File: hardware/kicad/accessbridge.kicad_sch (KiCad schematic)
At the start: 64 parts, among them J1 PWR+RELAY, J2 BELL+DPS, J3 Qwiic, J4 OUT, J5 EXP, Q1 AO3400A, SW1 PAIR, U1 AP63205WU-7, U2 XIAO_ESP32C6, U3 EL357N(C)(TA)-G, U4 EL357N(C)(TA)-G, U5 EL357N(C)(TA)-G, U6 CPC1014NTR

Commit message: HW-1.1 Rev B: USB-C power input; 3D-printable enclosure (DIN + wall)
- J6 power-only USB-C (5.1k CC, 500 mA PTC, SMAJ5.0A), diode-OR into the
  XIAO 5V pin and a new V_LOOP rail for the contact loops
- Board widened to 96 x 56 mm; Rev A placement and routing kept,
  incremental update/lock workflow in gen_pcb.py
- Regenerated fabrication data (HW-1.1 Rev B ZIP, BOM, CPL, renders, STEP)
- Parametric CadQuery enclosure: DIN-rail base, wall-screw base, lid,
  PAIR plunger, cable clamp; fit check against the PCB STEP; CI job
- Docs, tests plan and changelog updated

Co-Authored-By: Claude Opus 5.5 <noreply@anthropic.com>
Claude-Session: https://claude.ai/code/session_017ugbcLJnibWHxuv1cA2VcH
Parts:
- added C11: 10u/25V, Capacitor_SMD:C_0805_2012Metric, symbol Device:C
- added D13, D15, D16: SS14, Diode_SMD:D_SMA, symbol Device:D_Schottky
- added D14: SMAJ5.0A, Diode_SMD:D_SMA, symbol Diode:SMAJ5.0A
- added F2: 500mA/30V, Fuse:Fuse_1206_3216Metric, symbol Device:Polyfuse
- added J6: USB-C 5V, Connector_USB:USB_C_Receptacle_GCT_USB4125-xx-x_6P_TopMnt_Horizontal, symbol Connector:USB_C_Receptacle_PowerOnly_6P
- added R22, R23: 5.1k, Resistor_SMD:R_0603_1608Metric, symbol Device:R
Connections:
- net +12V: now also D15.2 (A); no longer R10.1, R14.1, R18.1
- net +5V_XIAO: now also D13.1 (K)
- net GND: now also C11.2, D14.2 (A2), J6.A12 (GND), J6.B12 (GND), J6.S1 (SHIELD), R22.2, R23.2
- new net CC1: J6.A5 (CC1), R22.1
- new net CC2: J6.B5 (CC2), R23.1
- new net VBUS: F2.1, J6.A9 (VBUS), J6.B9 (VBUS)
- new net VBUS_F: C11.1, D13.2 (A), D14.1 (A1), D16.2 (A), F2.2
- new net V_LOOP: D15.1 (K), D16.1 (K), R10.1, R14.1, R18.1
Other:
- note added: "CONTACT INPUTS: opto loops powered from V_LOOP (+12 V or USB 5 V)"
- note added: "Field loops: V_LOOP -> 2.2k -> opto LED -> COM ... contact ... NO -> 1k -> GND (~3.3 mA at 12 V, ~1.1 mA on USB)."
- note added: "J6 USB-C (Rev B): 5 V power only, no data. Firmware upload uses the XIAO's own USB-C."
- note added: "USB-C POWER INPUT 5 V (power only, Rev B)"
- note added: "VBUS -> F2 -> D13 -> +5V_XIAO (OR with D3) and D16 -> V_LOOP (OR with D15 from +12V). J4 OUT+ is 12 V only."
- note removed: "CONTACT INPUTS: opto loops powered from board +12 V (no external voltage)"
- note removed: "Field loops: +12V -> 2.2k -> opto LED -> COM ... contact ... NO -> 1k -> GND (~3.3 mA)."

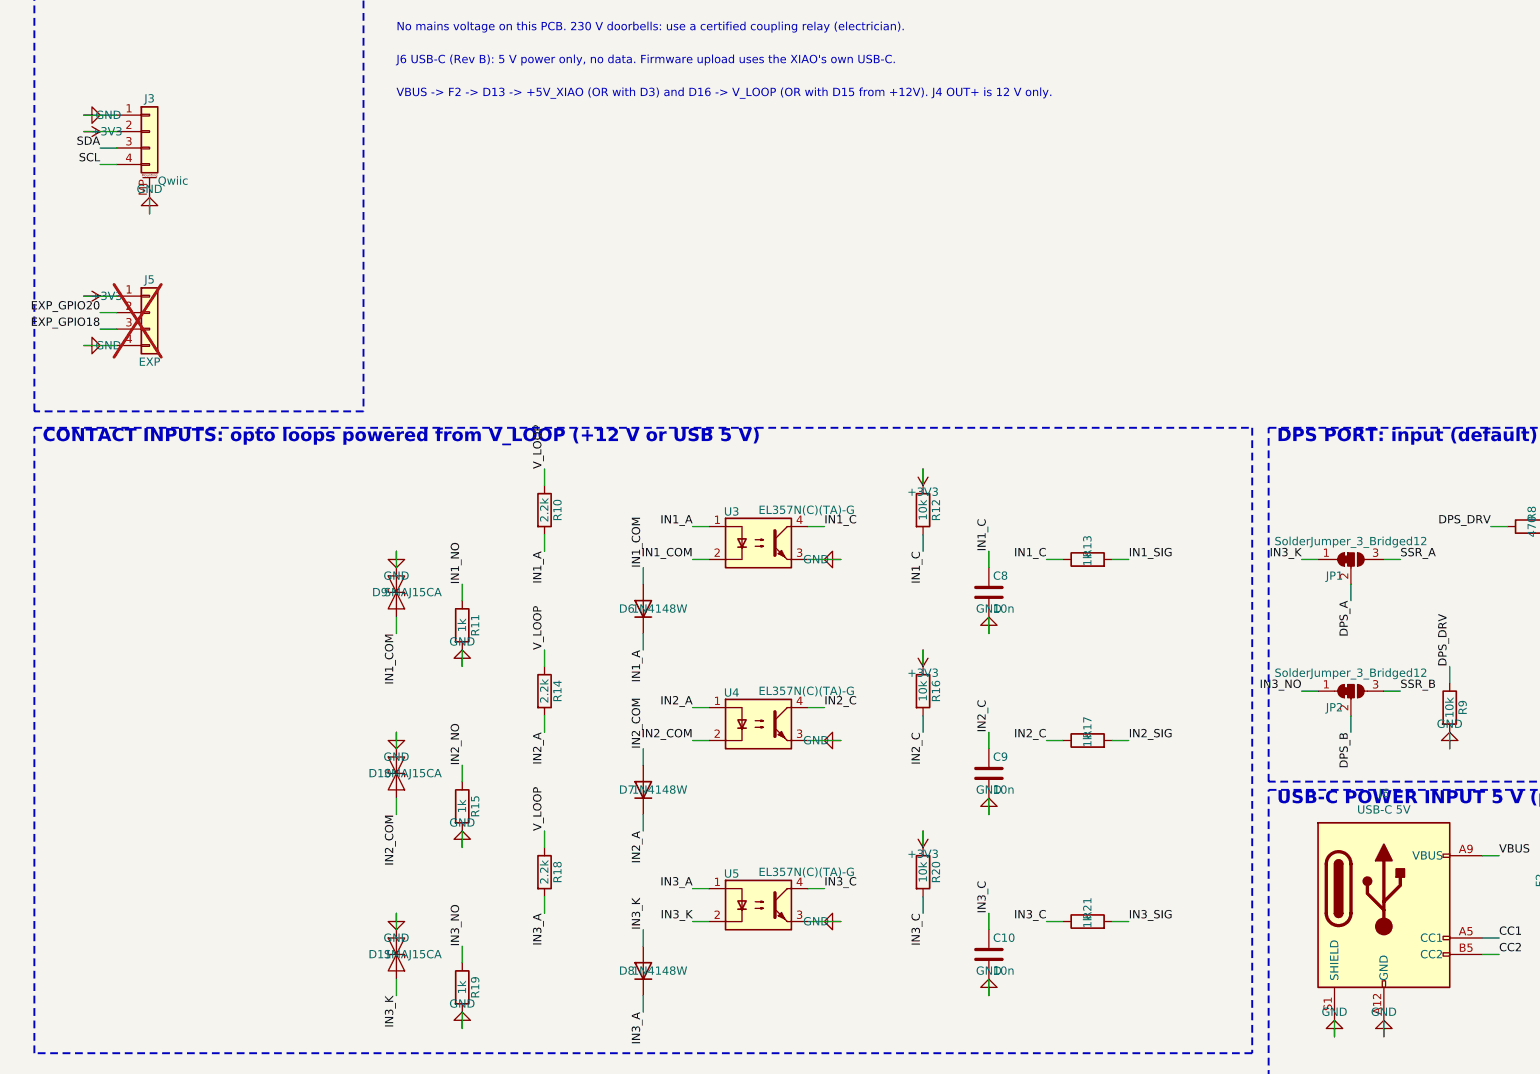
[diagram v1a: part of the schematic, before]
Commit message: Doorbell: any-source blueprint, no-neutral wiring options; wetting-current jumpers
- doorbell-notify blueprint accepts the AccessBridge counter, an event entity
  (e.g. Shelly input) or a binary sensor (e.g. battery Zigbee contact sensor);
  restore/reconnect ignored, optional event-type filter; 3 new tests (15/15)
- wiring.md: doorbell routes for 230 V bells without neutral at the push
  (coupling relay at the bell + battery Zigbee sensor, or cable to J2);
  Shelly 1L/2L and Eltako ER61-UC limitations documented
- Rev B (not manufactured): JP3-JP5 + R24-R26 (1k 1206, C4410) select ~3.3 or
  ~6 mA loop current per input; incremental routing, ERC/DRC clean incl. parity
- Regenerated fabrication data, renders, PCB STEP; enclosure fit check passes

Co-Authored-By: Claude Opus 5.5 <noreply@anthropic.com>
Claude-Session: https://claude.ai/code/session_017ugbcLJnibWHxuv1cA2VcH
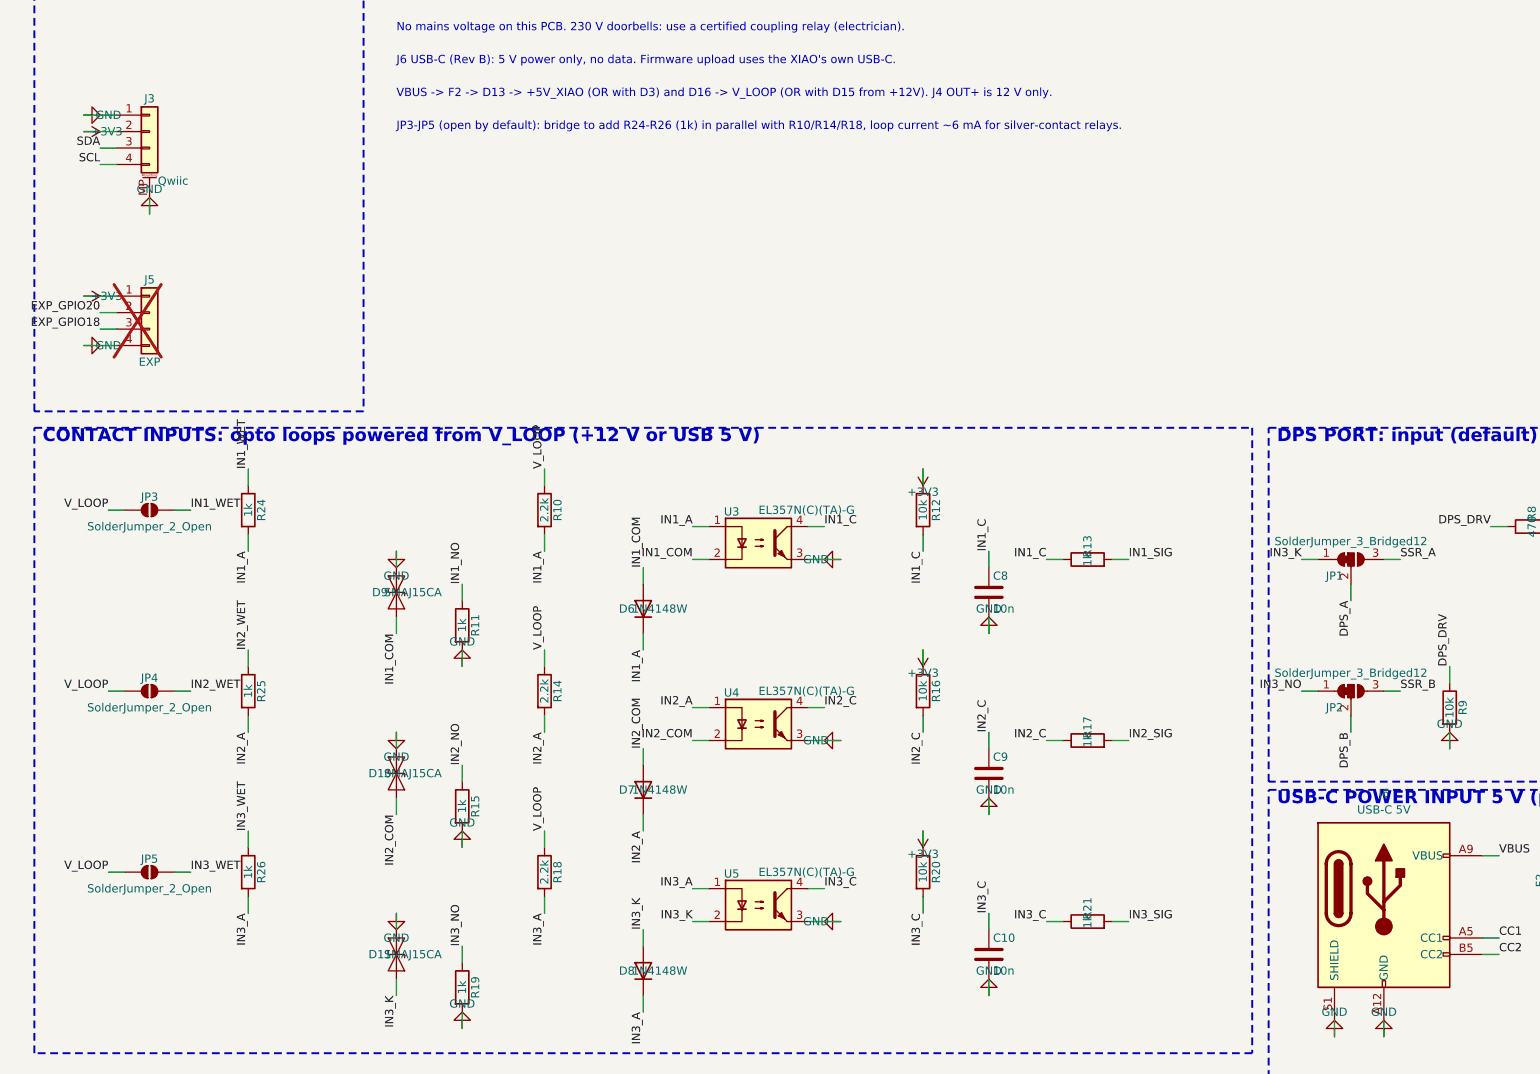
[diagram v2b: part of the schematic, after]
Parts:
- added JP3, JP4, JP5: SolderJumper_2_Open, Jumper:SolderJumper-2_P1.3mm_Open_RoundedPad1.0x1.5mm, symbol Jumper:SolderJumper_2_Open
- added R24, R25, R26: 1k, Resistor_SMD:R_1206_3216Metric, symbol Device:R
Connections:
- net IN1_A: now also R24.2
- net IN2_A: now also R25.2
- net IN3_A: now also R26.2
- net V_LOOP: now also JP3.1 (A), JP4.1 (A), JP5.1 (A)
- new net IN1_WET: JP3.2 (B), R24.1
- new net IN2_WET: JP4.2 (B), R25.1
- new net IN3_WET: JP5.2 (B), R26.1
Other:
- note added: "JP3-JP5 (open by default): bridge to add R24-R26 (1k) in parallel with R10/R14/R18, loop current ~6 mA for silver-contact relays."

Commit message: BOM: R8 470R = UNI-ROYAL 0603WAF4700T5E (C23179)
Co-Authored-By: Claude Opus 5.5 <noreply@anthropic.com>
Claude-Session: https://claude.ai/code/session_017ugbcLJnibWHxuv1cA2VcH
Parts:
- R8: LCSC (none) -> C23179; LCSC_Status unverified -> confirmed; MPN 0603 470R 1% thick film -> 0603WAF4700T5E; Manufacturer generic -> UNI-ROYAL
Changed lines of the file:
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@@
 			)
 		)
-		(property "MPN" "0603 470R 1% thick film"
+		(property "MPN" "0603WAF4700T5E"
 			(at 243.84 200.66 0)
 			(effects
@@
 			)
 		)
-		(property "Manufacturer" "generic"
+		(property "Manufacturer" "UNI-ROYAL"
 			(at 243.84 200.66 0)
 			(effects
@@
 			)
 		)
-		(property "LCSC" ""
+		(property "LCSC" "C23179"
 			(at 243.84 200.66 0)
 			(effects
@@
 			)
 		)
-		(property "LCSC_Status" "unverified"
+		(property "LCSC_Status" "confirmed"
 			(at 243.84 200.66 0)
 			(effects

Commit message: BOM: optocouplers U3-U5 = UMW EL357C (C725794); sync footprint values on update
Co-Authored-By: Claude Opus 5.5 <noreply@anthropic.com>
Claude-Session: https://claude.ai/code/session_017ugbcLJnibWHxuv1cA2VcH
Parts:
- U3, U4, U5: value EL357N(C)(TA)-G -> EL357C; LCSC C29981 -> C725794; MPN EL357N(C)(TA)-G -> EL357C; Manufacturer Everlight -> UMW
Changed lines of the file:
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@@
 			)
 		)
-		(property "Value" "EL357N(C)(TA)-G"
+		(property "Value" "EL357C"
 			(at 124.46 198.12 0)
 			(effects
@@
 			)
 		)
-		(property "MPN" "EL357N(C)(TA)-G"
+		(property "MPN" "EL357C"
 			(at 124.46 203.2 0)
 			(effects
@@
 			)
 		)
-		(property "Manufacturer" "Everlight"
+		(property "Manufacturer" "UMW"
 			(at 124.46 203.2 0)
 			(effects
@@
 			)
 		)
-		(property "LCSC" "C29981"
+		(property "LCSC" "C725794"
 			(at 124.46 203.2 0)
 			(effects
@@
 			)
 		)
-		(property "Value" "EL357N(C)(TA)-G"
+		(property "Value" "EL357C"
 			(at 124.46 226.06 0)
 			(effects
@@
 			)
 		)
-		(property "MPN" "EL357N(C)(TA)-G"
+		(property "MPN" "EL357C"
 			(at 124.46 231.14 0)
 			(effects
@@
 			)
 		)
-		(property "Manufacturer" "Everlight"
+		(property "Manufacturer" "UMW"
 			(at 124.46 231.14 0)
 			(effects
@@
 			)
 		)
-		(property "LCSC" "C29981"
+		(property "LCSC" "C725794"
 			(at 124.46 231.14 0)
 			(effects
@@
 			)
 		)
-		(property "Value" "EL357N(C)(TA)-G"
+		(property "Value" "EL357C"
 			(at 124.46 254 0)
 			(effects
@@
 			)
 		)
-		(property "MPN" "EL357N(C)(TA)-G"
+		(property "MPN" "EL357C"
 			(at 124.46 259.08 0)
 			(effects
@@
 			)
 		)
-		(property "Manufacturer" "Everlight"
+		(property "Manufacturer" "UMW"
 			(at 124.46 259.08 0)
 			(effects
@@
 			)
 		)
-		(property "LCSC" "C29981"
+		(property "LCSC" "C725794"
 			(at 124.46 259.08 0)
 			(effects

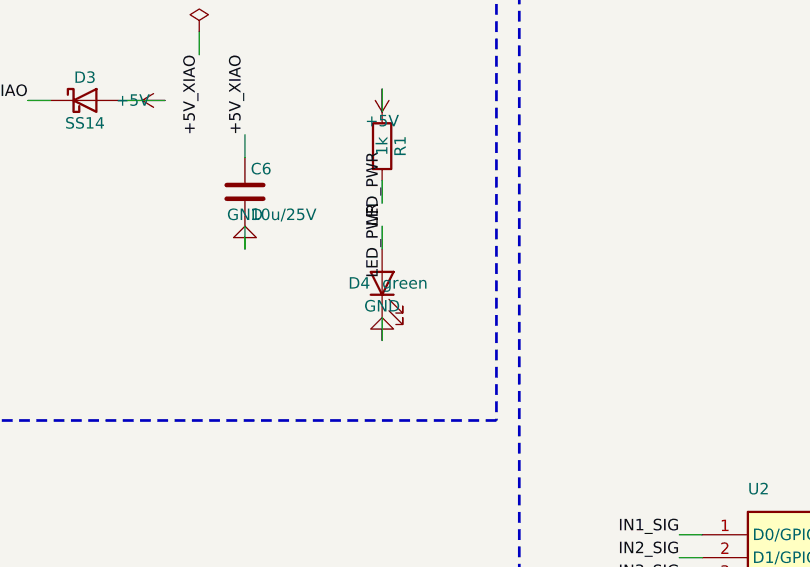
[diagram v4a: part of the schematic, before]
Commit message: BOM: D4 PWR LED = KT-0603YG yellow-green (C2289), green 0603 out of stock
Co-Authored-By: Claude Opus 5.5 <noreply@anthropic.com>
Claude-Session: https://claude.ai/code/session_017ugbcLJnibWHxuv1cA2VcH
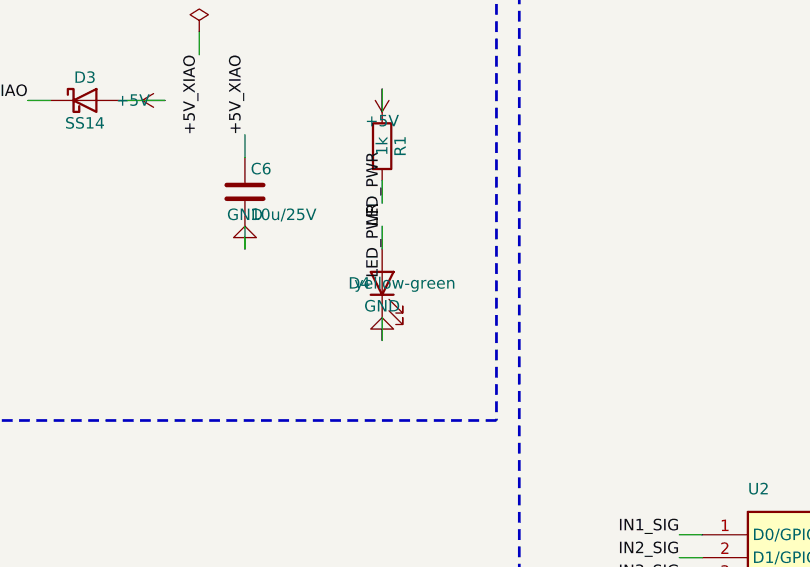
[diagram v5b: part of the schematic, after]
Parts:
- D4: value green -> yellow-green; LCSC C72043 -> C2289; LCSC_Status secondary -> confirmed; MPN KT-0603G (emerald) -> KT-0603YG
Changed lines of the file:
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@@
 			)
 		)
-		(property "Value" "green"
+		(property "Value" "yellow-green"
 			(at 299.72 66.04 90)
 			(effects
@@
 			)
 		)
-		(property "MPN" "KT-0603G (emerald)"
+		(property "MPN" "KT-0603YG"
 			(at 297.18 66.04 0)
 			(effects
@@
 			)
 		)
-		(property "LCSC" "C72043"
+		(property "LCSC" "C2289"
 			(at 297.18 66.04 0)
 			(effects
@@
 			)
 		)
-		(property "LCSC_Status" "secondary"
+		(property "LCSC_Status" "confirmed"
 			(at 297.18 66.04 0)
 			(effects
